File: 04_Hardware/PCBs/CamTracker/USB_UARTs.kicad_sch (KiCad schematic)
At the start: 38 parts, among them J3 67996-100HLF, J4 22-28-4034, J5 22-28-4034, J6 USB4080-03-A, U1 SC206EEMDA-G51-UGNDA

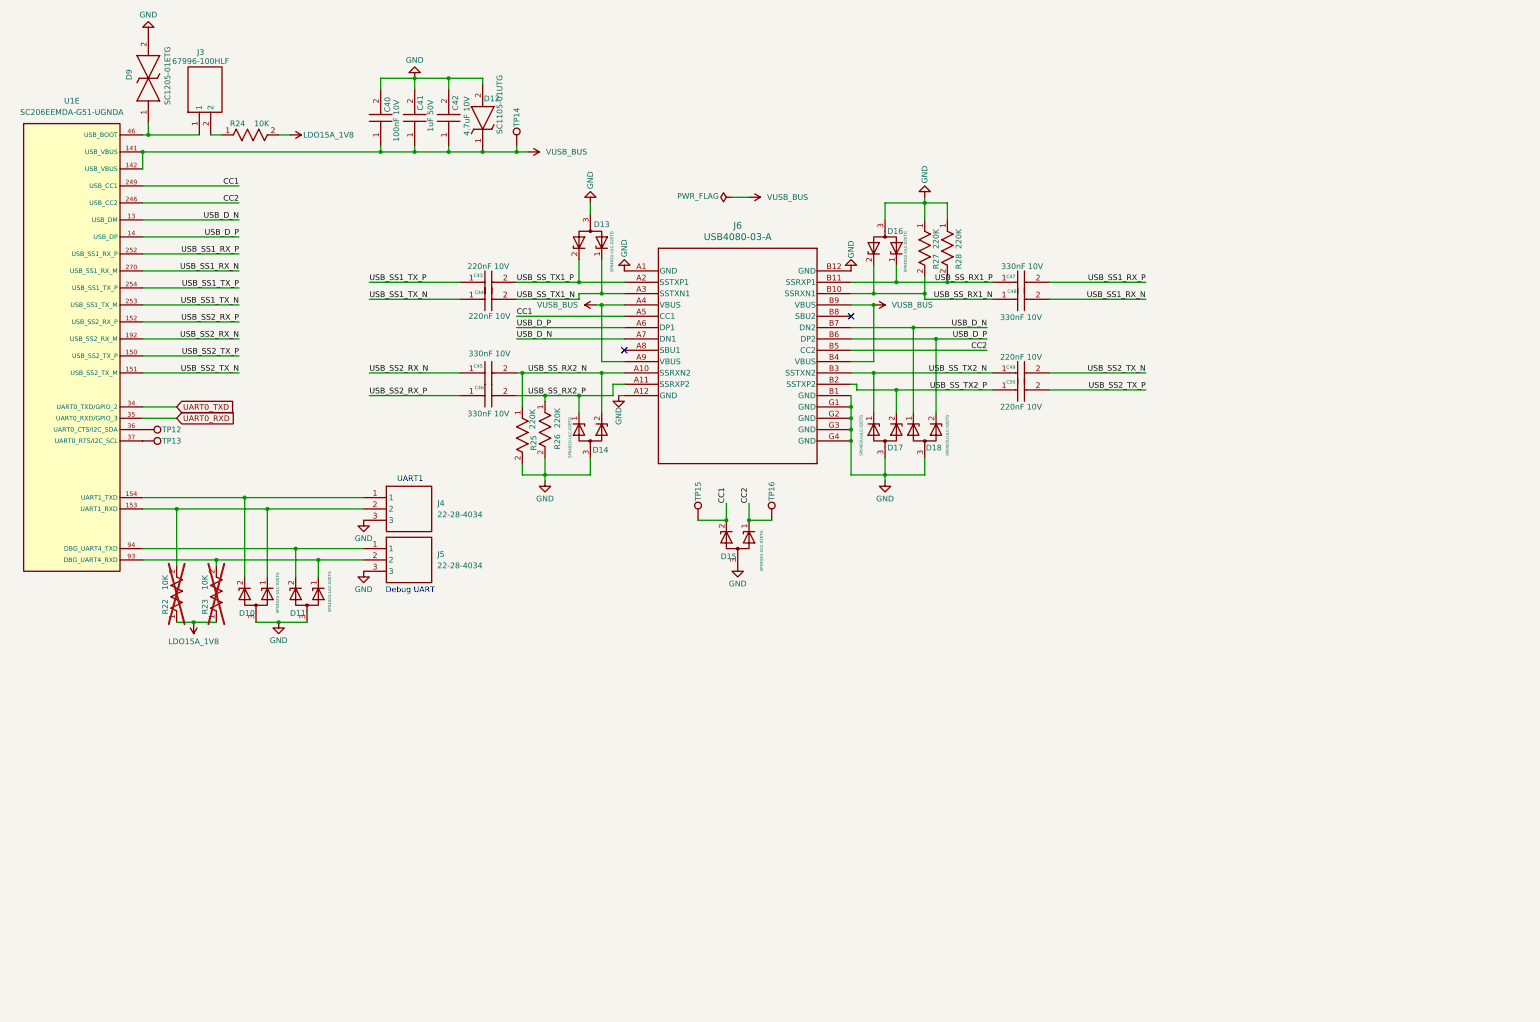
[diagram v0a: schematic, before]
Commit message: feat: Completed Placement v1 in Layout
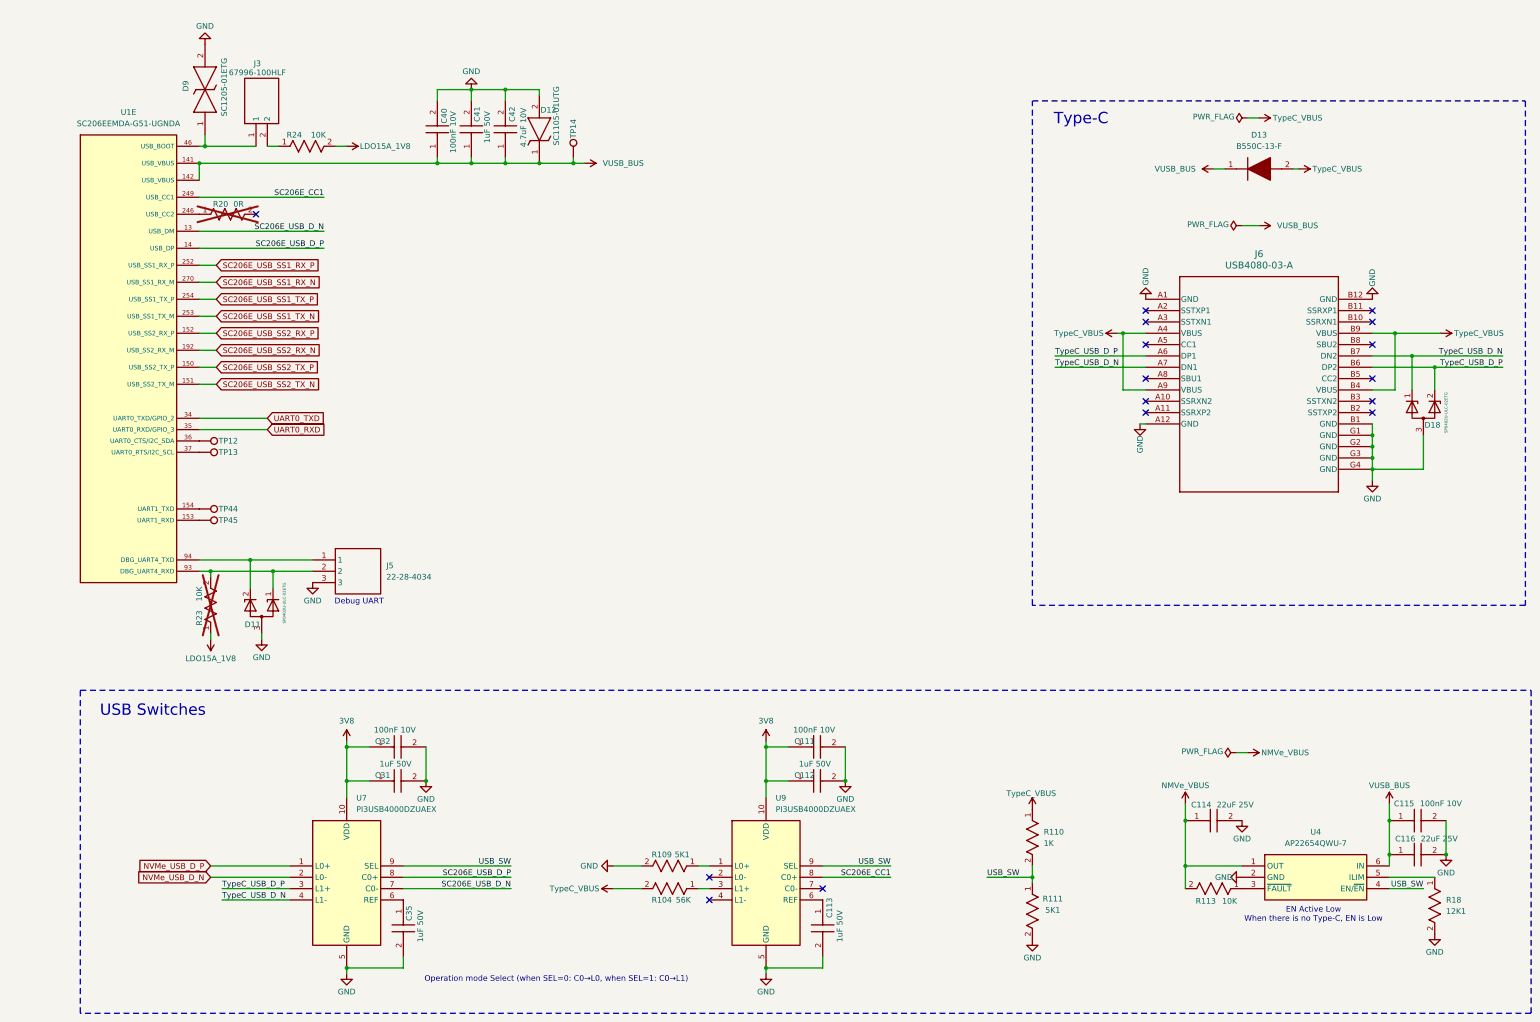
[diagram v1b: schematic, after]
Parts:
- removed C43, C44, C49, C50: 220nF 10V, 000MCLib:CAPC1005X55N, symbol 000MCLib:GRM155R61A224JE19D
- removed C45, C46, C47, C48: 330nF 10V, 000MCLib:CAPC1005X55N, symbol 000MCLib:GRM155R61A334KE15D
- removed D10, D13, D14, D15, D16, D17: SP0402U-ULC-02ETG, 000MCLib:SESD0402Q2UG0020090, symbol 000MCLib:SP0402U-ULC-02ETG
- removed J4: 22-28-4034, 000MCLib:HDRV3W66P0X254_1X3_762X249X1042P, symbol 000MCLib:22-28-4034
- removed R22: 10K, 000MCLib:RC0402N_YAG, symbol 000MCLib:RC0402JR-0710KL
- removed R25, R26, R27, R28: 220K, 000MCLib:RC0402N_YAG, symbol 000MCLib:RC0402FR-07220KL
- removed TP15, TP16: TestPoint, TestPoint:TestPoint_Pad_D1.0mm, symbol 000MCLib:TestPoint
- added C111, C115, C32: 100nF 10V, 000MCLib:CAPC1005X55N, symbol 000MCLib:GRM155R71A104KA01D
- added C112, C113, C31, C35: 1uF 50V, 000MCLib:CAPC1005X55N, symbol 000MCLib:GRM155R61H105KE05D
- added C114, C116: 22uF 25V, 000MCLib:CAPC2012X145N, symbol 000MCLib:GRM21BR61E226ME44L
- added D13: B550C-13-F, 000MCLib:DIOM7959X250N, symbol 000MCLib:B550C-13-F
- added R104: 56K, 000MCLib:RC0402N_YAG, symbol 000MCLib:RC0402JR-0756KL
- added R109, R111: 5K1, 000MCLib:RC0402N_YAG, symbol 000MCLib:RC0402JR-075K1L
- added R110: 1K, 000MCLib:RC0402N_YAG, symbol 000MCLib:RC0402JR-071KL
- added R113: 10K, 000MCLib:RC0402N_YAG, symbol 000MCLib:RC0402JR-0710KL
- added R18: 12K1, 000MCLib:RC0402N_YAG, symbol 000MCLib:RT1206FRE0712K1L
- added R20: 0R, 000MCLib:RESC2012X50N, symbol 000MCLib:CRCW08050000Z0EA
- added TP44, TP45: TestPoint, TestPoint:TestPoint_Pad_D1.0mm, symbol 000MCLib:TestPoint
- added U4: AP22654QWU-7, 000MCLib:SOT95P280X82-6N, symbol 000MCLib:AP22654QWU-7
- added U7, U9: PI3USB4000DZUAEX, 000MCLib:PI3USB4000DZUAEX, symbol 000MCLib:PI3USB4000DZUAEX
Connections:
- net GND: now also C111.2, C112.2, C113.2, C114.2, C115.2, C116.2, C31.2, C32.2, C35.2, R109.2, R111.2, R18.2, U4.2 (GND), U7.5 (GND), U9.5 (GND)
- net VUSB_BUS: now also C115.1, C116.1, D13.1 (K), U4.6 (IN); no longer J6.A4 (VBUS), J6.A9 (VBUS), J6.B4 (VBUS), J6.B9 (VBUS)
- net at U1.154 (UART1_TXD): now also TP44.1
- net at U1.153 (UART1_RXD): now also TP45.1
- net CC1: no longer names the net of J6.A5 (CC1)
- net CC1: no longer U1.249 (USB_CC1)
- net CC2: no longer names the net of U1.246 (USB_CC2)
- net CC2: now also R20.1; no longer J6.B5 (CC2)
- net USB_D_N renamed TypeC_USB_D_N
- net TypeC_USB_D_N: now also U7.4 (L1-); no longer U1.13 (USB_DM)
- net USB_D_P renamed TypeC_USB_D_P
- net TypeC_USB_D_P: now also U7.3 (L1+); no longer U1.14 (USB_DP)
- net USB_SS1_RX_N renamed SC206E_USB_SS1_RX_N
- net USB_SS1_RX_P renamed SC206E_USB_SS1_RX_P
- net USB_SS1_TX_N renamed SC206E_USB_SS1_TX_N
- net USB_SS1_TX_P renamed SC206E_USB_SS1_TX_P
- net USB_SS2_RX_N renamed SC206E_USB_SS2_RX_N
- net USB_SS2_RX_P renamed SC206E_USB_SS2_RX_P
- net USB_SS2_TX_N renamed SC206E_USB_SS2_TX_N
- net USB_SS2_TX_P renamed SC206E_USB_SS2_TX_P
- net USB_SS_RX1_N: no longer names the net of J6.B10 (SSRXN1)
- net USB_SS_RX1_P: no longer names the net of J6.B11 (SSRXP1)
- net USB_SS_RX2_N: no longer names the net of J6.A10 (SSRXN2)
- net USB_SS_RX2_P: no longer names the net of J6.A11 (SSRXP2)
- net USB_SS_TX1_N: no longer names the net of J6.A3 (SSTXN1)
- net USB_SS_TX1_P: no longer names the net of J6.A2 (SSTXP1)
- net USB_SS_TX2_N: no longer names the net of J6.B3 (SSTXN2)
- net USB_SS_TX2_P: no longer names the net of J6.B2 (SSTXP2)
- new net: R109.1, U9.1 (L0+)
- new net: R104.1, U9.3 (L1+)
- new net: C113.1, U9.6 (REF)
- new net: R113.1, U4.3 (~{FAULT})
- new net: R18.1, U4.5 (ILIM)
- new net: C35.1, U7.6 (REF)
- new net 3V8: C111.1, C112.1, C31.1, C32.1, U7.10 (VDD), U9.10 (VDD)
- new net NMVe_VBUS: C114.1, R113.2, U4.1 (OUT)
- new net NVMe_USB_D_N: U7.2 (L0-)
- new net NVMe_USB_D_P: U7.1 (L0+)
- new net SC206E_CC1: U1.249 (USB_CC1), U9.8 (C0+)
- new net SC206E_USB_D_N: U1.13 (USB_DM), U7.7 (C0-)
- new net SC206E_USB_D_P: U1.14 (USB_DP), U7.8 (C0+)
- new net TypeC_VBUS: D13.2 (A), J6.A4 (VBUS), J6.A9 (VBUS), J6.B4 (VBUS), J6.B9 (VBUS), R104.2, R110.1
- new net USB_SW: R110.2, R111.1, U4.4 (EN/~{EN}), U7.9 (SEL), U9.9 (SEL)
- no-connect marks 2 -> 16
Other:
- note added: "EN Active Low When there is no Type-C, EN is Low"
- note added: "Operation mode Select (when SEL=0: C0→L0, when SEL=1: C0→L1)"
- note added: "Type-C"
- note added: "USB Switches"
- note removed: "UART1"
- moved on the sheet: C40, C41, C42, D11, D12, D18, D9, J3, J5, J6, R23, R24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

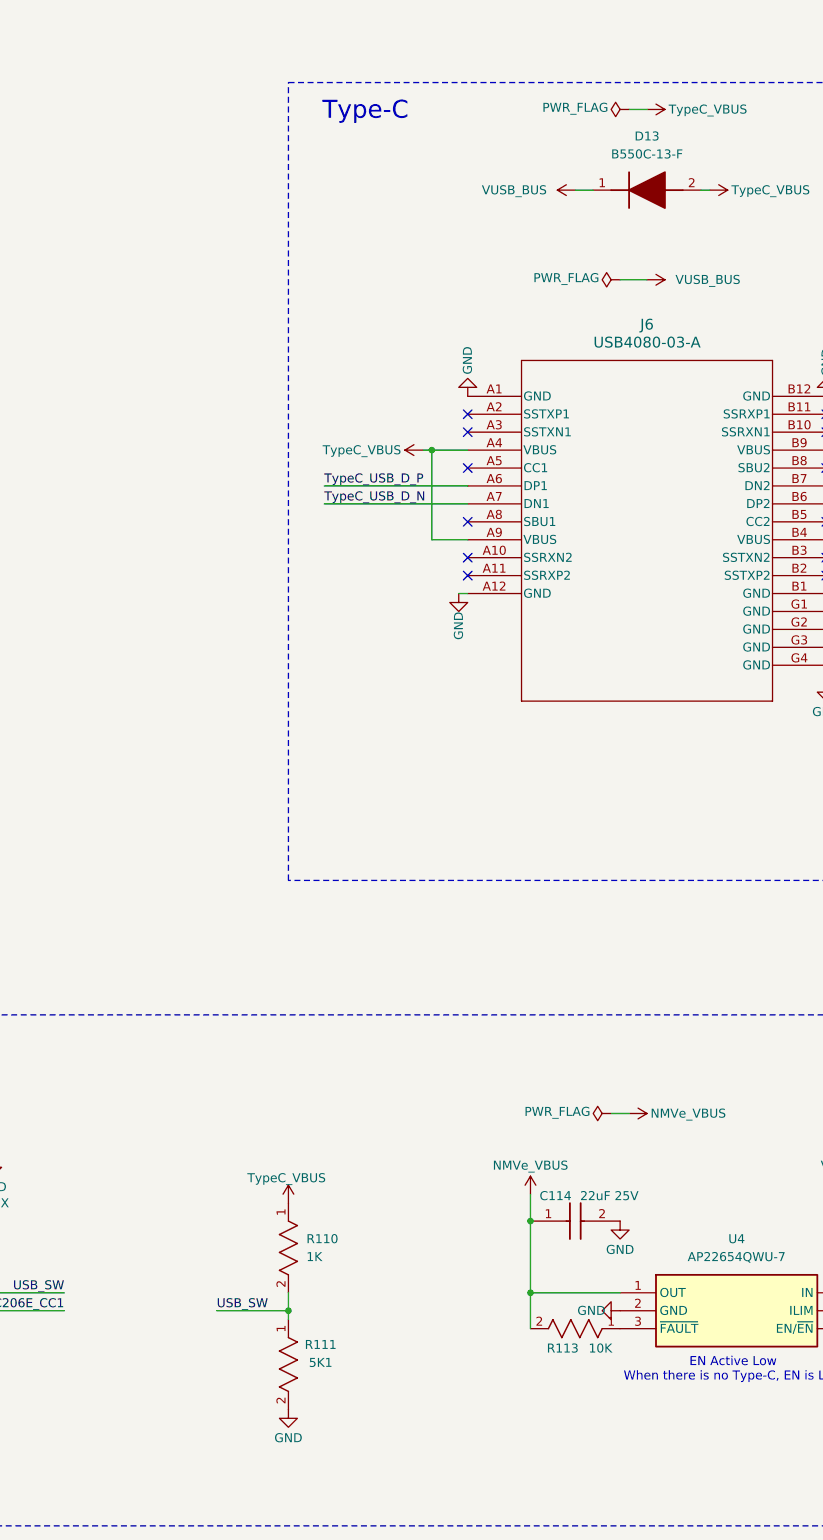
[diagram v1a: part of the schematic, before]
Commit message: feat(layout): Completed Layout Design with new Camera Connectors
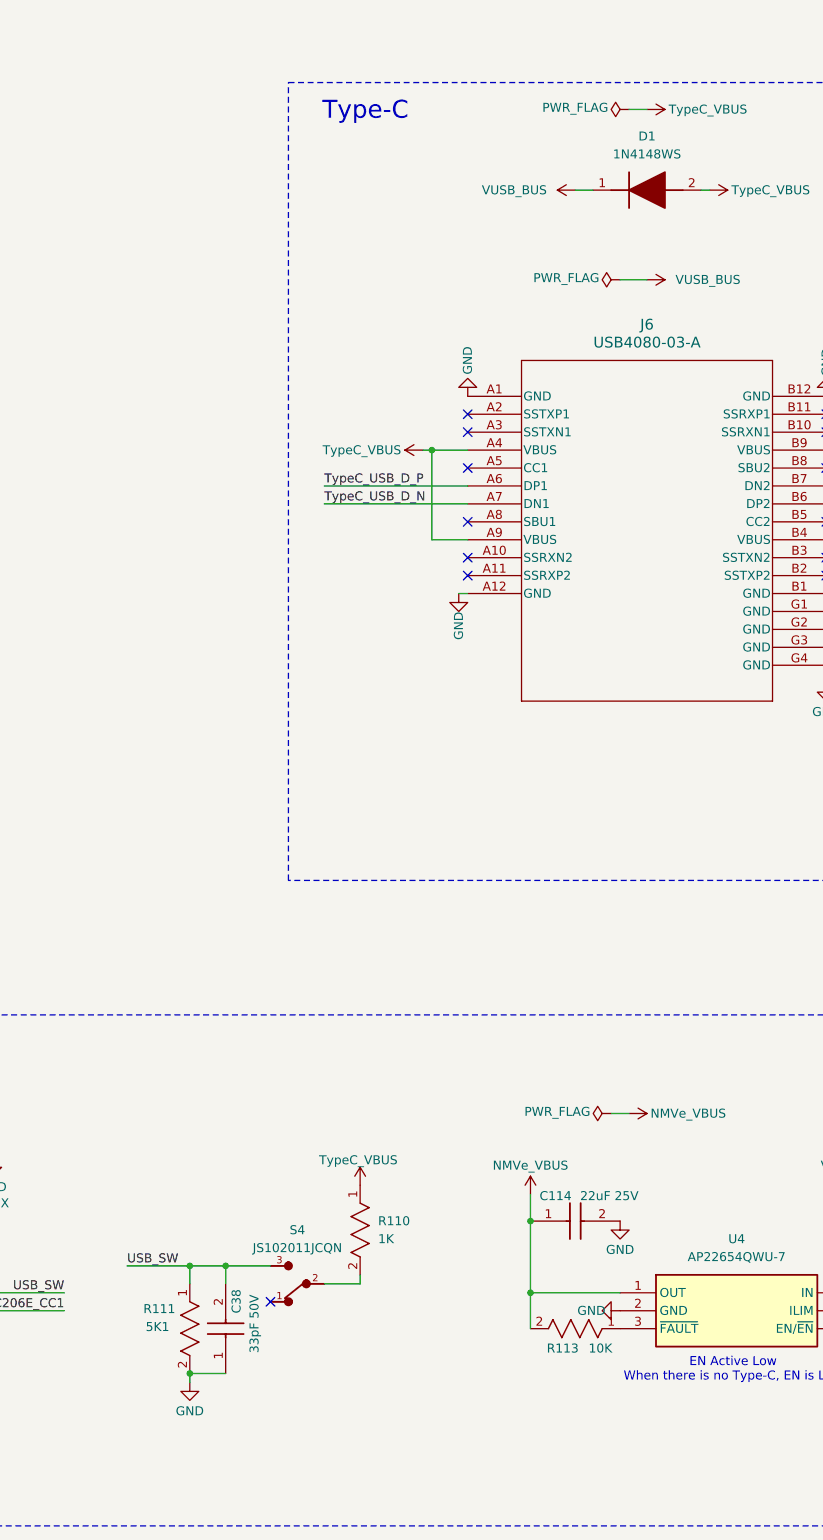
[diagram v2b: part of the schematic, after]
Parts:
- removed D13: B550C-13-F, 000MCLib:DIOM7959X250N, symbol 000MCLib:B550C-13-F
- added C38: 33pF 50V, 000MCLib:CAPC1005X55N, symbol 000MCLib:GRM1555C1H330JA01D
- added D1: 1N4148WS, 000MCLib:SODFL2512X90N, symbol 000MCLib:1N4148WS
- added S4: JS102011JCQN, 000MCLib:SW_JS102011JCQN, symbol 000MCLib:JS102011JCQN
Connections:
- net GND: now also C38.1
- net TypeC_VBUS: now also D1.2 (A)
- net USB_SW: now also C38.2, S4.3; no longer R110.2
- net VUSB_BUS: now also D1.1 (K)
- new net: R110.2, S4.2
- no-connect marks 16 -> 17
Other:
- moved on the sheet: R110, R111

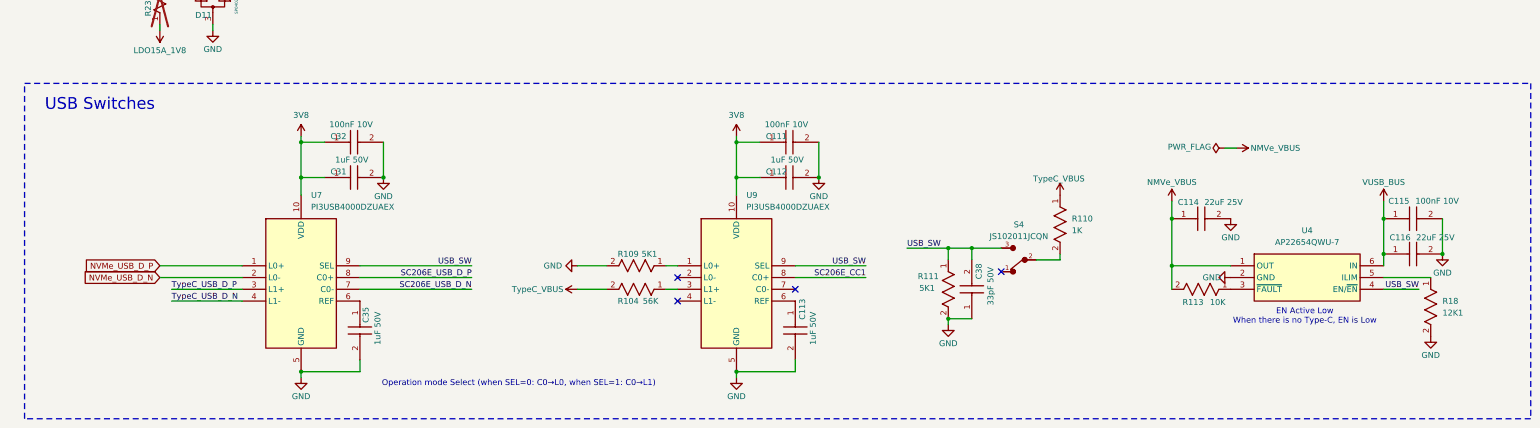
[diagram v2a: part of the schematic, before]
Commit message: feat(PCB): Finalized design and generated Gerber files and BOM
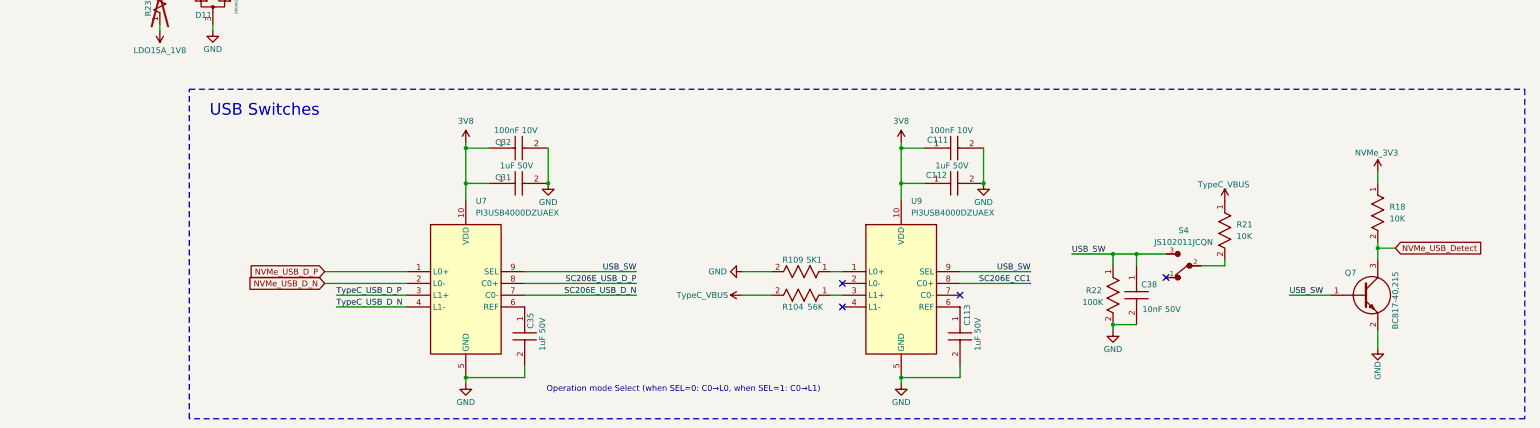
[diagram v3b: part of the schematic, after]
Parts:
- removed C114, C116: 22uF 25V, 000MCLib:CAPC2012X145N, symbol 000MCLib:GRM21BR61E226ME44L
- removed C115: 100nF 10V, 000MCLib:CAPC1005X55N, symbol 000MCLib:GRM155R71A104KA01D
- removed C38: 33pF 50V, 000MCLib:CAPC1005X55N, symbol 000MCLib:GRM1555C1H330JA01D
- removed R110: 1K, 000MCLib:RC0402N_YAG, symbol 000MCLib:RC0402JR-071KL
- removed R111: 5K1, 000MCLib:RC0402N_YAG, symbol 000MCLib:RC0402JR-075K1L
- removed R113: 10K, 000MCLib:RC0402N_YAG, symbol 000MCLib:RC0402JR-0710KL
- removed R18: 12K1, 000MCLib:RC0402N_YAG, symbol 000MCLib:RT1206FRE0712K1L
- removed U4: AP22654QWU-7, 000MCLib:SOT95P280X82-6N, symbol 000MCLib:AP22654QWU-7
- added C38: 10nF 50V, 000MCLib:CAPC1005X55N, symbol 000MCLib:GRM155R71H103KA88D
- added Q7: BC817-40,215, 000MCLib:BC81740215, symbol 000MCLib:BC817-40,215
- added R18, R21: 10K, 000MCLib:RC0402N_YAG, symbol 000MCLib:RC0402JR-0710KL
- added R22: 100K, 000MCLib:RC0402N_YAG, symbol 000MCLib:RC0402JR-07100KL
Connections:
- net GND: now also C38.2, Q7.2 (E), R22.2
- net TypeC_VBUS: now also R21.1
- net USB_SW: now also C38.1, Q7.1 (B), R22.1
- net at S4.2: now also R21.2
- new net NVMe_3V3: R18.1
- new net NVMe_USB_Detect: Q7.3 (C), R18.2
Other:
- note removed: "EN Active Low When there is no Type-C, EN is Low"
- moved on the sheet: C111, C112, C113, C31, C32, C35, R104, R109, S4, U7, U9
